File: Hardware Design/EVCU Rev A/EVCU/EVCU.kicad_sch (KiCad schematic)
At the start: 62 parts

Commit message: scemes
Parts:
- gave numbers to parts that had none: 61
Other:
- note added: "CANBUS Tranceiver and CANBUS DB9 connector"
- note removed: "CANBUS Tranceiver & CANBUS DB9 connector"
- note removed: "SET GRID TO 2.54mm"

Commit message: poeosp
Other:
- note added: "APPS"
- note removed: "Accelerator Pedal Position Sensor"
- company: (none) -> University of Alberta Formula Racing
- title: (none) -> Electric Vehicle Control Unit
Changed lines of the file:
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@@
 (kicad_sch (version 20211123) (generator eeschema)
   (paper "A2")
+  (title_block
+    (title "Electric Vehicle Control Unit")
+    (date "2022-11-18")
+    (rev "A")
+    (company "University of Alberta Formula Racing")
+  )
   (junction (at 325.12 289.56) (diameter 0) (color 0 0 0 0)
   )
@@
     (effects (font (size 3 3)) (justify left bottom))
   )
-  (text "Accelerator Pedal Position Sensor" (at 439.42 170.18 0)
+  (text "APPS\n" (at 439.42 170.18 0)
     (effects (font (size 3 3)) (justify left bottom))
   )

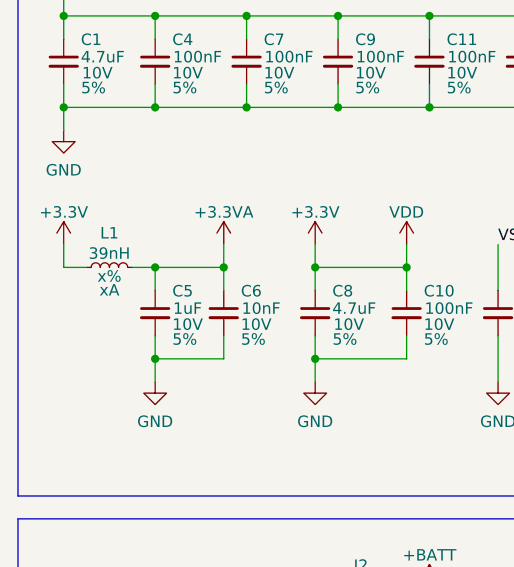
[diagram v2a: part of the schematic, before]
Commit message: inductor rating
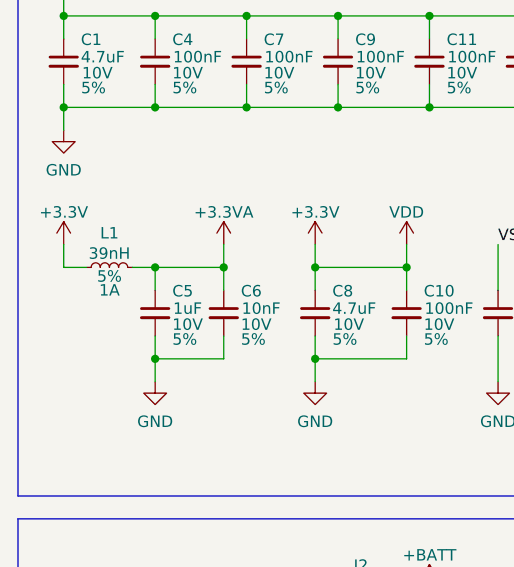
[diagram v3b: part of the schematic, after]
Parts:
- L1: Rating xA -> 1A; Tolerance x% -> 5%
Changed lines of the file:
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@@
       (effects (font (size 1.27 1.27)) hide)
     )
-    (property "Rating" "xA" (id 4) (at 22.86 53.34 90))
-    (property "Tolerance" "x%" (id 5) (at 22.86 51.8 90))
+    (property "Rating" "1A" (id 4) (at 22.86 53.34 90))
+    (property "Tolerance" "5%" (id 5) (at 22.86 51.8 90))
     (pin "1")
     (pin "2")

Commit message: pung
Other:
- note added: "SET GRID TO 2.54mm"
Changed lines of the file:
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@@
     (effects (font (size 3 3)) (justify left bottom))
+  )
+  (text "SET GRID TO 2.54mm\n" (at -17.78 17.78 0)
+    (effects (font (size 40 40)) (justify left bottom))
   )
   (label "LMBOUT" (at 525.78 134.62 0)

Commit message: op
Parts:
- added D?: ESDA6V1BC6, Package_TO_SOT_SMD:SOT-23-6, symbol Power_Protection:ESDA6V1BC6
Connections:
- new net: D?.2 (COM), D?.5 (COM)
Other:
- moved on the sheet: C20, C21, R1, U3, X1

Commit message: CANBUS esd
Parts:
- removed D?: ESDA6V1BC6, Package_TO_SOT_SMD:SOT-23-6, symbol Power_Protection:ESDA6V1BC6
- added U9: ESDCAN24-2BLY, Package_TO_SOT_SMD:SC-59, symbol Power_Protection:ESDCAN24-2BLY
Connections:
- net CAN_H: now also U9.2
- net CAN_L: now also U9.1
- net GND: now also U9.3
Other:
- moved on the sheet: R10, R6, R7, U6

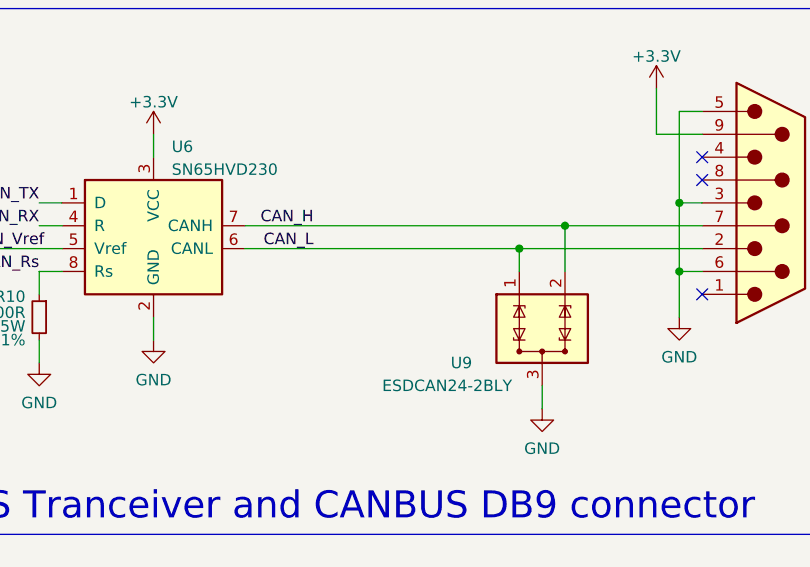
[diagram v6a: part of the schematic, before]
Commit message: 120R resistor for CANH_L
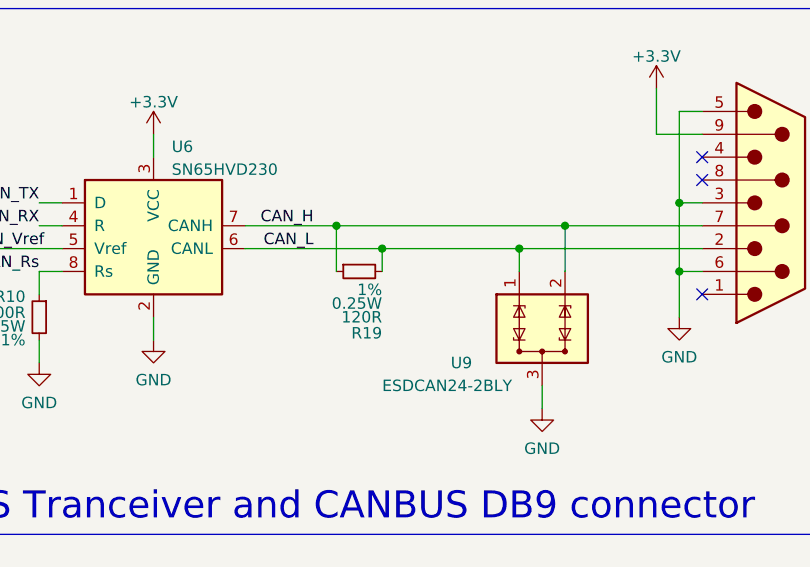
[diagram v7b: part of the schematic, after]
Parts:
- added R19: 120R, symbol Device:R_Small
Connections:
- net CAN_H: now also R19.1
- net CAN_L: now also R19.2
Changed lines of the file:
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@@
   (junction (at 63.5 134.62) (diameter 0) (color 0 0 0 0)
   )
+  (junction (at 520.7 40.64) (diameter 0) (color 0 0 0 0)
+  )
   (junction (at 525.78 322.58) (diameter 0) (color 0 0 0 0)
   )
@@
   (junction (at 546.1 149.86) (diameter 0) (color 0 0 0 0)
   )
+  (junction (at 515.62 38.1) (diameter 0) (color 0 0 0 0)
+  )
   (junction (at 515.62 259.08) (diameter 0) (color 0 0 0 0)
   )
@@
     (stroke (width 0) (type default) (color 0 0 0 0))
   )
-  (wire (pts (xy 505.46 38.1) (xy 541.02 38.1))
+  (wire (pts (xy 505.46 38.1) (xy 515.62 38.1))
     (stroke (width 0) (type default) (color 0 0 0 0))
   )
@@
     (stroke (width 0) (type default) (color 0 0 0 0))
   )
+  (wire (pts (xy 515.62 38.1) (xy 515.62 43.18))
+    (stroke (width 0) (type default) (color 0 0 0 0))
+  )
   (wire (pts (xy 535.94 40.64) (xy 535.94 43.18))
     (stroke (width 0) (type default) (color 0 0 0 0))
@@
     (stroke (width 0) (type default) (color 0 0 0 0))
   )
+  (wire (pts (xy 520.7 40.64) (xy 520.7 43.18))
+    (stroke (width 0) (type default) (color 0 0 0 0))
+  )
   (wire (pts (xy 515.62 259.08) (xy 515.62 261.62))
     (stroke (width 0) (type default) (color 0 0 0 0))
@@
     (stroke (width 0) (type default) (color 0 0 0 0))
   )
+  (wire (pts (xy 520.7 40.64) (xy 535.94 40.64))
+    (stroke (width 0) (type default) (color 0 0 0 0))
+  )
   (wire (pts (xy 279.4 88.9) (xy 279.4 91.44))
     (stroke (width 0) (type default) (color 0 0 0 0))
@@
     (stroke (width 0) (type default) (color 0 0 0 0))
   )
-  (wire (pts (xy 505.46 40.64) (xy 535.94 40.64))
-    (stroke (width 0) (type default) (color 0 0 0 0))
-  )
   (wire (pts (xy 233.68 142.24) (xy 256.54 142.24))
     (stroke (width 0) (type default) (color 0 0 0 0))
@@
     (stroke (width 0) (type default) (color 0 0 0 0))
   )
+  (wire (pts (xy 505.46 40.64) (xy 520.7 40.64))
+    (stroke (width 0) (type default) (color 0 0 0 0))
+  )
   (polyline (pts (xy 119.38 76.2) (xy 12.7 76.2))
     (stroke (width 0) (type default) (color 0 0 0 0))
@@
     (stroke (width 0) (type default) (color 0 0 0 0))
   )
+  (wire (pts (xy 515.62 38.1) (xy 541.02 38.1))
+    (stroke (width 0) (type default) (color 0 0 0 0))
+  )
   (polyline (pts (xy 193.04 66.04) (xy 345.44 66.04))
     (stroke (width 0) (type default) (color 0 0 0 0))
@@
     (pin "2")
   )
+  (symbol (lib_id "Device:R_Small") (at 518.16 43.18 90) (mirror x) (unit 1)
+    (in_bom yes) (on_board yes)
+    (property "Reference" "R19" (id 0) (at 520.7 50.038 90)
+      (effects (font (size 1.27 1.27)) (justify left))
+    )
+    (property "Value" "120R" (id 1) (at 520.7 48.26 90)
+      (effects (font (size 1.27 1.27)) (justify left))
+    )
+    (property "Footprint" "" (id 2) (at 518.16 43.18 0)
+      (effects (font (size 1.27 1.27)) hide)
+    )
+    (property "Datasheet" "~" (id 3) (at 518.16 43.18 0)
+      (effects (font (size 1.27 1.27)) hide)
+    )
+    (property "Rating" "0.25W" (id 4) (at 520.7 46.736 90)
+      (effects (font (size 1.27 1.27)) (justify left))
+    )
+    (property "Tolerance" "1%" (id 5) (at 520.7 45.212 90)
+      (effects (font (size 1.27 1.27)) (justify left))
+    )
+    (pin "1")
+    (pin "2")
+  )
   (symbol (lib_id "power:+3.3V") (at 45.72 48.26 0) (unit 1)
     (in_bom yes) (on_board yes) (fields_autoplaced)
@@
     (pin "2")
     (pin "3")
-    (pin "5")
-    (pin "6")
-    (pin "7")
-    (pin "4")
-    (pin "8")
   )
   (symbol (lib_id "Device:R_Small") (at 464.82 203.2 0) (mirror y) (unit 1)
@@
     (pin "2")
     (pin "3")
-    (pin "5")
-    (pin "6")
-    (pin "7")
-    (pin "4")
-    (pin "8")
   )
   (symbol (lib_id "Device:R_Small") (at 495.3 203.2 0) (mirror y) (unit 1)
@@
       (effects (font (size 1.27 1.27)) hide)
     )
-    (pin "1")
-    (pin "2")
-    (pin "3")
-    (pin "5")
-    (pin "6")
-    (pin "7")
     (pin "4")
     (pin "8")
@@
       (reference "R18") (unit 1) (value "100kR") (footprint "")
     )
+    (path "/62488973-4ad6-4e20-b6a8-734835a108dc"
+      (reference "R19") (unit 1) (value "120R") (footprint "")
+    )
     (path "/f520a214-9533-4cc8-af07-b67dc05e3b2a"

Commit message: esd protection
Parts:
- removed R2, R3, R4, R5: 10kR, symbol Device:R_Small
- added C29: C_Small, symbol Device:C_Small
- added D1: D_Zener, Diode_SMD:D_SMB_Handsoldering, symbol Device:D_Zener
- added U10: EMIF06-MSD02N16, Diode_SMD:EMIF06-MSD02N16, symbol Diode:EMIF06-MSD02N16
- added U11: ESDALC6V1W5, Package_TO_SOT_SMD:SOT-353_SC-70-5_Handsoldering, symbol Power_Protection:ESDALC6V1W5
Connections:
- net +3V3: now also C29.1, D1.1 (K), U10.15 (VCC), U10.16 (RDATA_VCC)
- net GND: now also C29.2, D1.2 (A), U10.17 (GND), U11.5
- net MISO: now also U10.10 (DAT0_Ex), U10.7 (DAT0_In)
- net MOSI: now also U10.12 (CMD_Ex), U10.5 (CMD_In)
- net SCK: now also U10.11 (CLK_Ex), U10.6 (CLK_In)
- net SD_CS: now also U10.13 (DAT3_EX), U10.4 (DAT3_In)
- net SWCLK: now also U11.4
- net SWDIO: now also U11.1
- no-connect marks 119 -> 127
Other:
- note added: "MCU Crystal Oscillator and SWD Connector"
- note removed: "MCU"
- note removed: "SWD and Power Connector"
- moved on the sheet: C12, C13, C2, C20, C21, C3, J1, J2, R1, U1, U2, U3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
